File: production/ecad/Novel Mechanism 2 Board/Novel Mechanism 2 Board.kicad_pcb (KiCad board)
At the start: 2 copper layers, 37.4 x 45 mm, 19 parts, among them J1 1755736, J2 1755736, J3 0532611271, U1 L9958SBTR, U2 TMCS1108A4BQDRQ1

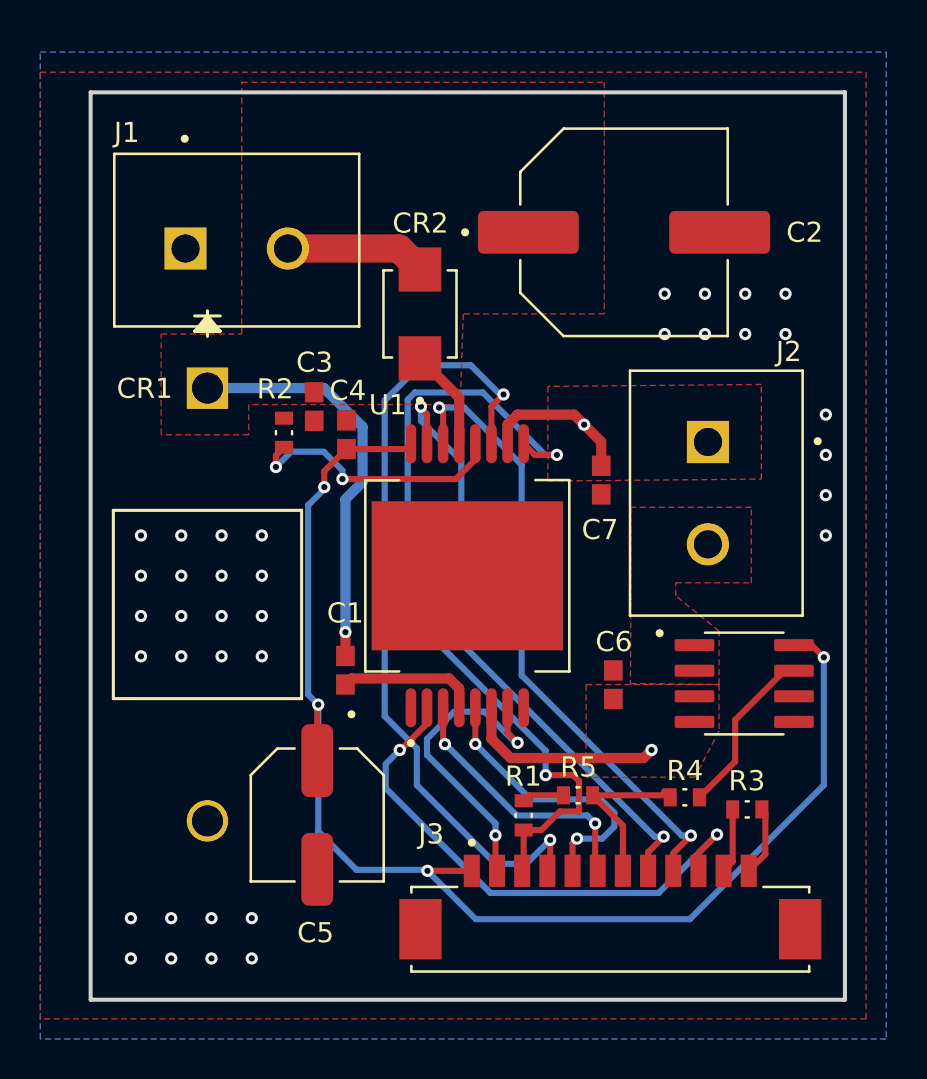
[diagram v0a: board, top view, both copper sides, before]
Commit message: added mounting holes
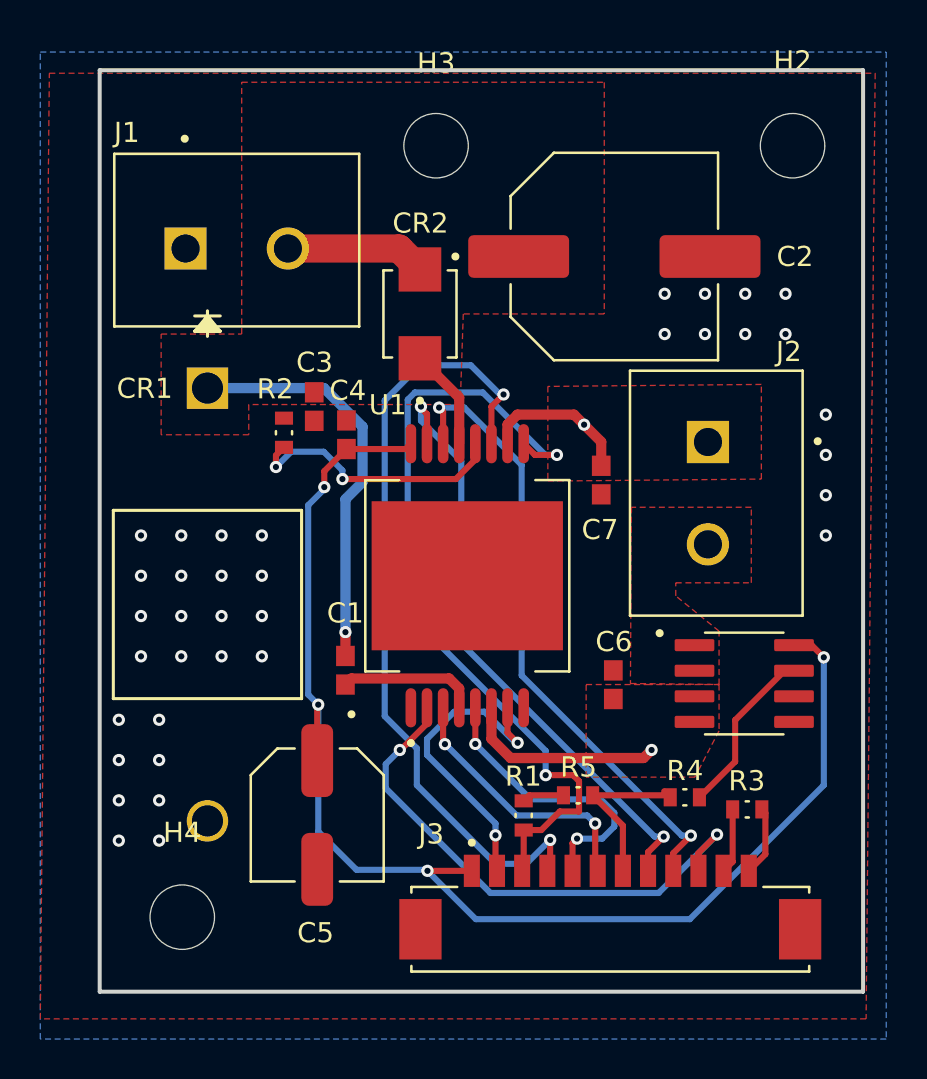
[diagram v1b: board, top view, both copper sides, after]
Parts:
- added H2: MountingHole, MountingHole:MountingHole_3.2mm_M3, F.Cu at (153.3, 48.6)
- added H3: MountingHole, MountingHole:MountingHole_3.2mm_M3, F.Cu at (135.7, 48.8)
- added H4: MountingHole, MountingHole:MountingHole_3.2mm_M3, F.Cu at (123.0, 87.0)
- moved C2 1.29 mm to (144.5, 54.1)
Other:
- board size 37.4 x 45 mm -> 37.9 x 45.8 mm
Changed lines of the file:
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@@
       (net 20 "/AOUT") (pintype "passive") (solder_mask_margin 0.102))
+  )
+  (footprint "MountingHole:MountingHole_3.2mm_M3" (layer "F.Cu")
+    (at 153.35 48.65)
+    (descr "Mounting Hole 3.2mm, no annular, M3")
+    (tags "mounting hole 3.2mm no annular m3")
+    (property "Sheetfile" "Novel Mechanism 2 Board.kicad_sch")
+    (property "Sheetname" "")
+    (property "ki_description" "Mounting Hole without connection")
+    (property "ki_keywords" "mounting hole")
+    (attr exclude_from_pos_files)
+    (fp_text reference "H2" (at 0 -4.2) (layer "F.SilkS")
+        (effects (font (size 1 1) (thickness 0.15)))
+    )
+    (fp_text value "MountingHole" (at 0 4.2) (layer "F.Fab")
+        (effects (font (size 1 1) (thickness 0.15)))
+    )
+    (fp_text user "${REFERENCE}" (at 0 0) (layer "F.Fab")
+        (effects (font (size 1 1) (thickness 0.15)))
+    )
+    (fp_circle (center 0 0) (end 3.2 0)
+      (stroke (width 0.15) (type solid)) (fill none) (layer "Cmts.User"))
+    (fp_circle (center 0 0) (end 3.45 0)
+      (stroke (width 0.05) (type solid)) (fill none) (layer "F.CrtYd"))
+    (pad "" np_thru_hole circle (at 0 0) (size 3.2 3.2) (drill 3.2) (layers "F&B.Cu" "*.Mask"))
   )
   (footprint "Capacitor_SMD:CAP_0603" (layer "F.Cu")
@@
       (net 5 "GND") (pinfunction "EXP") (pintype "passive") (solder_mask_margin 0.102))
   )
+  (footprint "MountingHole:MountingHole_3.2mm_M3" (layer "F.Cu")
+    (at 123.05 86.95)
+    (descr "Mounting Hole 3.2mm, no annular, M3")
+    (tags "mounting hole 3.2mm no annular m3")
+    (property "Sheetfile" "Novel Mechanism 2 Board.kicad_sch")
+    (property "Sheetname" "")
+    (property "ki_description" "Mounting Hole without connection")
+    (property "ki_keywords" "mounting hole")
+    (attr exclude_from_pos_files)
+    (fp_text reference "H4" (at 0 -4.2) (layer "F.SilkS")
+        (effects (font (size 1 1) (thickness 0.15)))
+    )
+    (fp_text value "MountingHole" (at 0 4.2) (layer "F.Fab")
+        (effects (font (size 1 1) (thickness 0.15)))
+    )
+    (fp_text user "${REFERENCE}" (at 0 0) (layer "F.Fab")
+        (effects (font (size 1 1) (thickness 0.15)))
+    )
+    (fp_circle (center 0 0) (end 3.2 0)
+      (stroke (width 0.15) (type solid)) (fill none) (layer "Cmts.User"))
+    (fp_circle (center 0 0) (end 3.45 0)
+      (stroke (width 0.05) (type solid)) (fill none) (layer "F.CrtYd"))
+    (pad "" np_thru_hole circle (at 0 0) (size 3.2 3.2) (drill 3.2) (layers "F&B.Cu" "*.Mask"))
+  )
   (footprint "Capacitor_SMD:EDK107M063A9PAA" (layer "F.Cu")
-    (at 144.98 52.95)
+    (at 144.5 54.15)
     (property "Sheetfile" "Novel Mechanism 2 Board.kicad_sch")
     (property "Sheetname" "")
@@
       (net 24 "unconnected-(J3-SHIELD__1-PadS2)") (pinfunction "SHIELD__1") (pintype "passive") (solder_mask_margin 0.0762))
   )
-  (gr_rect (start 118.5 46) (end 155.95 91.05)
+  (footprint "MountingHole:MountingHole_3.2mm_M3" (layer "F.Cu")
+    (at 135.65 48.75)
+    (descr "Mounting Hole 3.2mm, no annular, M3")
+    (tags "mounting hole 3.2mm no annular m3")
+    (property "Sheetfile" "Novel Mechanism 2 Board.kicad_sch")
+    (property "Sheetname" "")
+    (property "ki_description" "Mounting Hole without connection")
+    (property "ki_keywords" "mounting hole")
+    (attr exclude_from_pos_files)
+    (fp_text reference "H3" (at 0 -4.2) (layer "F.SilkS")
+        (effects (font (size 1 1) (thickness 0.15)))
+    )
+    (fp_text value "MountingHole" (at 0 4.2) (layer "F.Fab")
+        (effects (font (size 1 1) (thickness 0.15)))
+    )
+    (fp_text user "${REFERENCE}" (at 0 0) (layer "F.Fab")
+        (effects (font (size 1 1) (thickness 0.15)))
+    )
+    (fp_circle (center 0 0) (end 3.2 0)
+      (stroke (width 0.15) (type solid)) (fill none) (layer "Cmts.User"))
+    (fp_circle (center 0 0) (end 3.45 0)
+      (stroke (width 0.05) (type solid)) (fill none) (layer "F.CrtYd"))
+    (pad "" np_thru_hole circle (at 0 -0.1) (size 3.2 3.2) (drill 3.2) (layers "F&B.Cu" "*.Mask"))
+  )
+  (gr_rect (start 118.95 44.9) (end 156.85 90.65)
     (stroke (width 0.2) (type default)) (fill none) (layer "Edge.Cuts"))
   (segment (start 136.8 61.155) (end 134.85 59.205) (width 0.508) (layer "F.Cu") (net 1))
@@
   (via (at 121 68) (size 0.6096) (drill 0.3048) (layers "F.Cu" "B.Cu") (free) (net 5))
   (via (at 121 74) (size 0.6096) (drill 0.3048) (layers "F.Cu" "B.Cu") (free) (net 5))
-  (via (at 122.5 89) (size 0.6096) (drill 0.3048) (layers "F.Cu" "B.Cu") (free) (net 5))
+  (via (at 121.9 81.15) (size 0.6096) (drill 0.3048) (layers "F.Cu" "B.Cu") (free) (net 5))
   (via (at 127 72) (size 0.6096) (drill 0.3048) (layers "F.Cu" "B.Cu") (free) (net 5))
   (via (at 153 58) (size 0.6096) (drill 0.3048) (layers "F.Cu" "B.Cu") (free) (net 5))
@@
   (via (at 151 58) (size 0.6096) (drill 0.3048) (layers "F.Cu" "B.Cu") (free) (net 5))
   (via (at 149 56) (size 0.6096) (drill 0.3048) (layers "F.Cu" "B.Cu") (free) (net 5))
-  (via (at 126.5 89) (size 0.6096) (drill 0.3048) (layers "F.Cu" "B.Cu") (free) (net 5))
+  (via (at 121.9 77.15) (size 0.6096) (drill 0.3048) (layers "F.Cu" "B.Cu") (free) (net 5))
   (via (at 147 56) (size 0.6096) (drill 0.3048) (layers "F.Cu" "B.Cu") (free) (net 5))
   (via (at 151 56) (size 0.6096) (drill 0.3048) (layers "F.Cu" "B.Cu") (free) (net 5))
@@
   (via (at 155 64) (size 0.6096) (drill 0.3048) (layers "F.Cu" "B.Cu") (free) (net 5))
   (via (at 127 68) (size 0.6096) (drill 0.3048) (layers "F.Cu" "B.Cu") (free) (net 5))
-  (via (at 122.5 87) (size 0.6096) (drill 0.3048) (layers "F.Cu" "B.Cu") (free) (net 5))
+  (via (at 119.9 81.15) (size 0.6096) (drill 0.3048) (layers "F.Cu" "B.Cu") (free) (net 5))
   (via (at 125 72) (size 0.6096) (drill 0.3048) (layers "F.Cu" "B.Cu") (free) (net 5))
-  (via (at 124.5 89) (size 0.6096) (drill 0.3048) (layers "F.Cu" "B.Cu") (free) (net 5))
+  (via (at 121.9 79.15) (size 0.6096) (drill 0.3048) (layers "F.Cu" "B.Cu") (free) (net 5))
   (via (at 123 70) (size 0.6096) (drill 0.3048) (layers "F.Cu" "B.Cu") (free) (net 5))
   (via (at 125 70) (size 0.6096) (drill 0.3048) (layers "F.Cu" "B.Cu") (free) (net 5))
@@
   (via (at 121 72) (size 0.6096) (drill 0.3048) (layers "F.Cu" "B.Cu") (free) (net 5))
   (via (at 127 74) (size 0.6096) (drill 0.3048) (layers "F.Cu" "B.Cu") (free) (net 5))
-  (via (at 124.5 87) (size 0.6096) (drill 0.3048) (layers "F.Cu" "B.Cu") (free) (net 5))
+  (via (at 119.9 79.15) (size 0.6096) (drill 0.3048) (layers "F.Cu" "B.Cu") (free) (net 5))
   (via (at 153 56) (size 0.6096) (drill 0.3048) (layers "F.Cu" "B.Cu") (free) (net 5))
   (via (at 123 68) (size 0.6096) (drill 0.3048) (layers "F.Cu" "B.Cu") (free) (net 5))
-  (via (at 126.5 87) (size 0.6096) (drill 0.3048) (layers "F.Cu" "B.Cu") (free) (net 5))
+  (via (at 119.9 77.15) (size 0.6096) (drill 0.3048) (layers "F.Cu" "B.Cu") (free) (net 5))
   (via (at 155 62) (size 0.6096) (drill 0.3048) (layers "F.Cu" "B.Cu") (free) (net 5))
-  (via (at 120.5 87) (size 0.6096) (drill 0.3048) (layers "F.Cu" "B.Cu") (free) (net 5))
+  (via (at 119.9 83.15) (size 0.6096) (drill 0.3048) (layers "F.Cu" "B.Cu") (free) (net 5))
   (via (at 149 58) (size 0.6096) (drill 0.3048) (layers "F.Cu" "B.Cu") (free) (net 5))
-  (via (at 120.5 89) (size 0.6096) (drill 0.3048) (layers "F.Cu" "B.Cu") (free) (net 5))
+  (via (at 121.9 83.15) (size 0.6096) (drill 0.3048) (layers "F.Cu" "B.Cu") (free) (net 5))
   (via (at 127 70) (size 0.6096) (drill 0.3048) (layers "F.Cu" "B.Cu") (free) (net 5))
   (segment (start 138.4 78.1) (end 138.4 76.555) (width 0.508) (layer "F.Cu") (net 6))
@@
     (polygon
       (pts
-        (xy 157 45)
+        (xy 157.45 45.05)
         (xy 157 92)
         (xy 116 92)
-        (xy 116 45)
-      )
-    )
+        (xy 116.45 45.05)
+      )
+    )

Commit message: final board edits
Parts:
- renumbered H3 to H1, H4 to H3
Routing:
- net Net-(U1-OUT1): track 10.1 -> 9.20 mm, vias 1 -> 0
- net Net-(U1-OUT2): track 7.31 -> 7.57 mm, vias 1 -> 0
- net GND: vias 36 -> 44
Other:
- board text added: "Sensify Drill Module by Hari N."
